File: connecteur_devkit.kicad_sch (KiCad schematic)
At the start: 8 parts, among them J10 OLED_SPI_2x8, J5 DEVKIT_C2000_ROW_A, J6 DEVKIT_C2000_ROW_B, J7 ESP32_C6_DEVKITC_1_J1, J8 ESP32_C6_DEVKITC_1_J3, U4 ER-OLEDM032-1

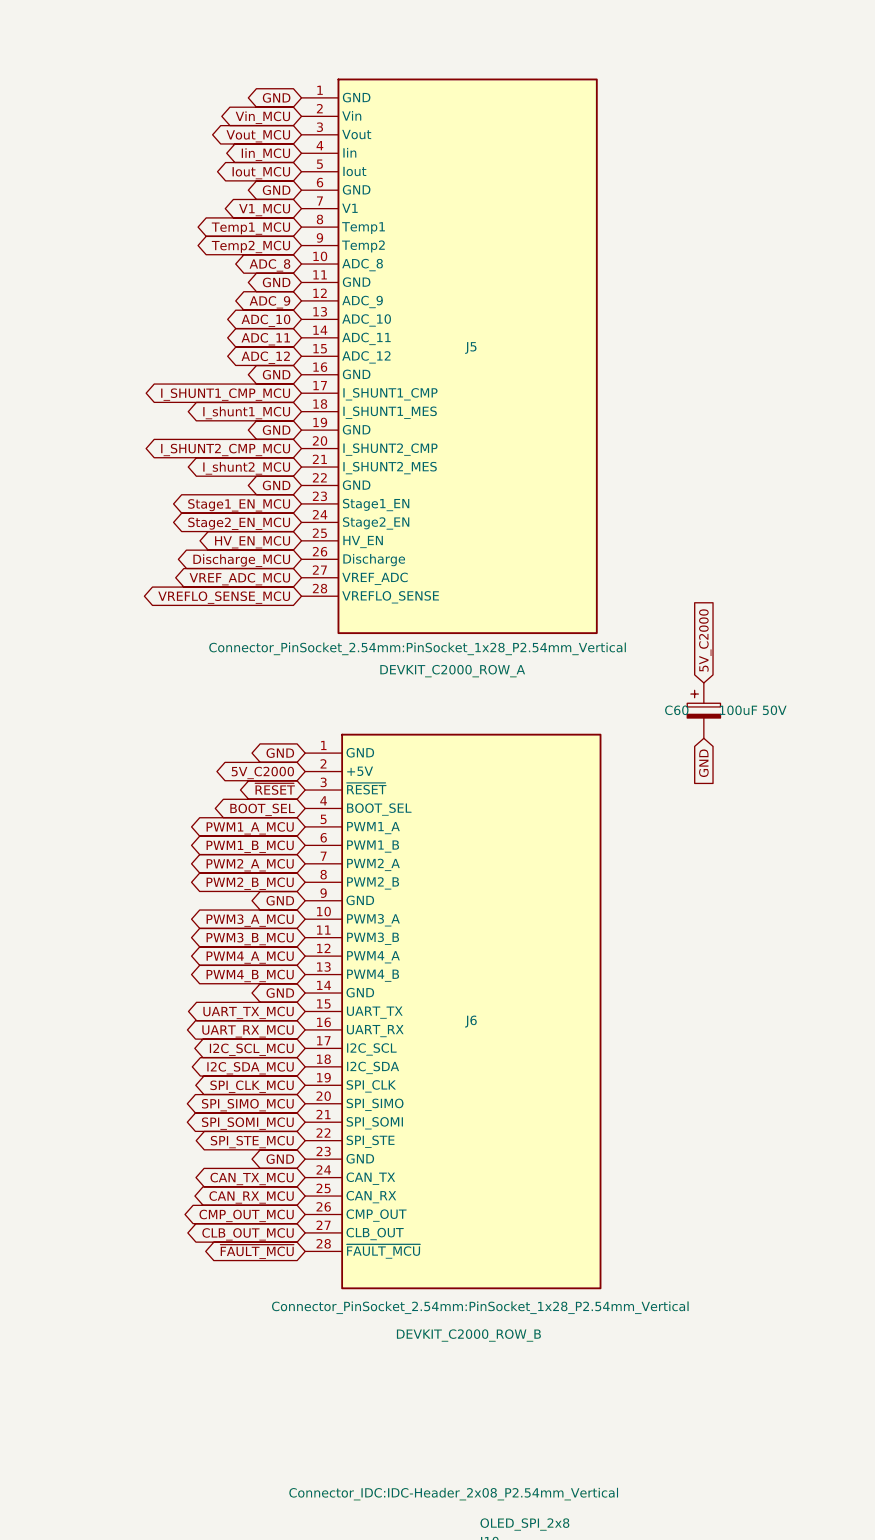
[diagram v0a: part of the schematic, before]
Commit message: Remplace le connecteur devkit par le nouveau connecteur devkit_B (2x24/2x24)
devkit_B_F28P551 est passe a deux embases 2x24 (une par domaine, masse
en vis-a-vis de chaque signal pour reduire l'inductance de boucle),
construit cote KICAD-C2000-devkit a partir du plan v2
(doc/connecteur-v2-plan.md la-bas). Remplace DEVKIT_C2000_ROW_A/ROW_B
(1x28 chacun) par DEVKIT_C2000_A/DEVKIT_C2000_B sur ce shield (J17/J18,
footprint PinSocket_2x24_P2.54mm_Vertical).

Remplacement pur : les 96 nouveaux noms de broche retombent tous dans
la table deja construite depuis les 56 anciennes etiquettes reelles
(verifie, pas suppose) - aucun renommage de net, aucune modification
attendue dans les nappes/protections. devkit_A_F280037 n'est plus
compatible avec ce shield tant qu'il n'a pas recu la meme mise a jour
(decision #25, meme logique que la decision #13 cote devkit).

Deux bugs trouves et corriges pendant la generation (noms de net bruts
au lieu des vrais noms projet avec suffixe _MCU ; broches no_connect
etiquetees au lieu d'un marqueur dedie) - voir decision #25 pour le
detail. Verifie avec check_schematic_labels.py et kicad-cli sch erc
feuille par feuille : aucune categorie nouvelle, aucune augmentation
ailleurs que sur les reserves deja connues.

Co-Authored-By: Claude Sonnet 5 <noreply@anthropic.com>
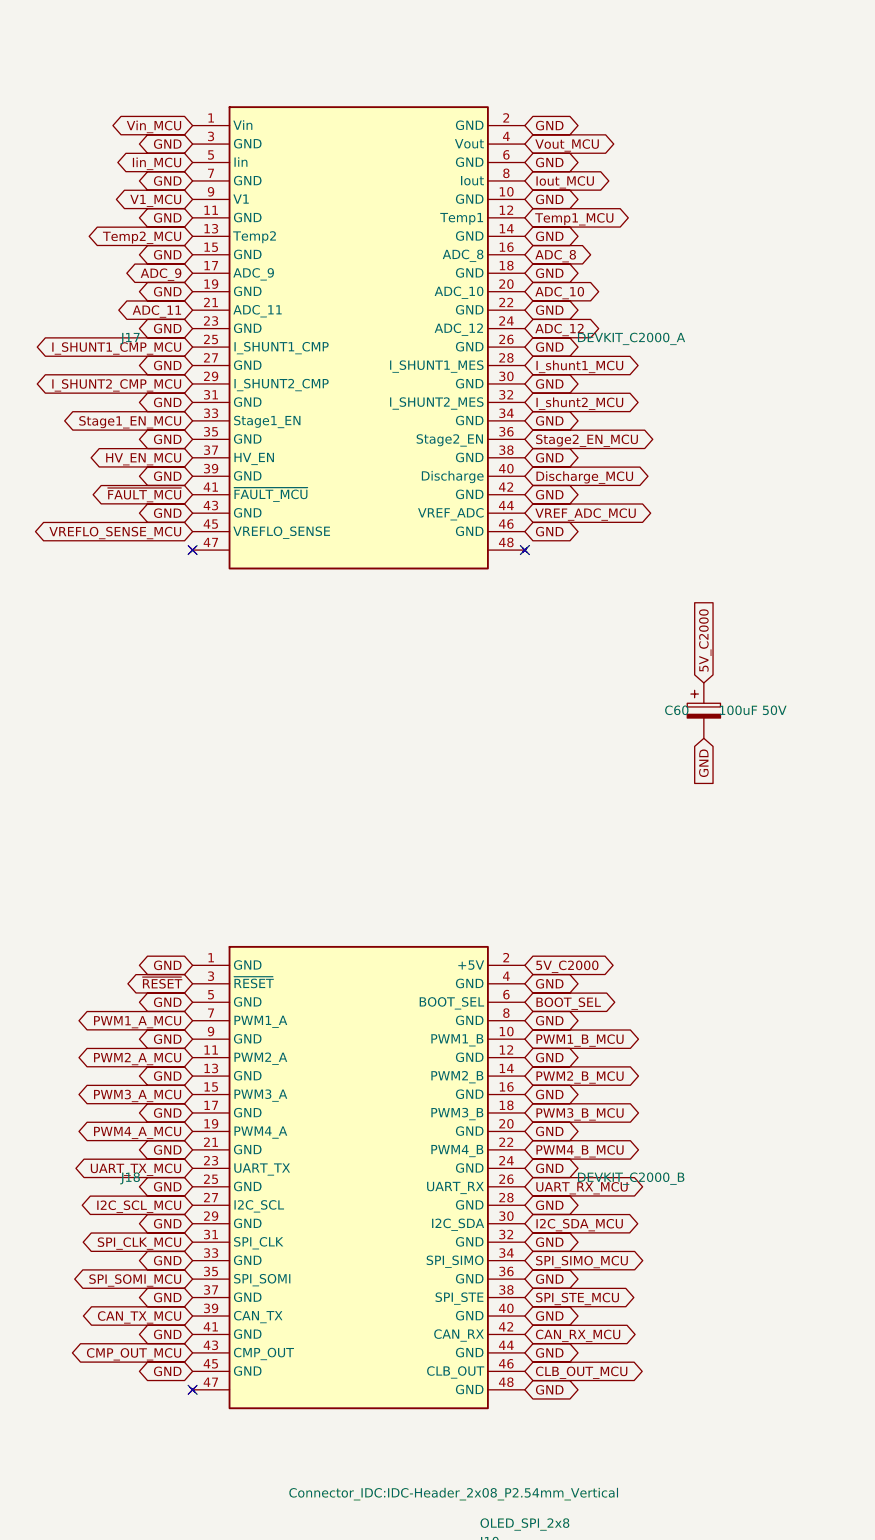
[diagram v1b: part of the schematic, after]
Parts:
- removed J5: DEVKIT_C2000_ROW_A, Connector_PinSocket_2.54mm:PinSocket_1x28_P2.54mm_Vertical, symbol C2000_Devkit_Connectors:DEVKIT_C2000_ROW_A
- removed J6: DEVKIT_C2000_ROW_B, Connector_PinSocket_2.54mm:PinSocket_1x28_P2.54mm_Vertical, symbol C2000_Devkit_Connectors:DEVKIT_C2000_ROW_B
- added J17: DEVKIT_C2000_A, Connector_PinSocket_2.54mm:PinSocket_2x24_P2.54mm_Vertical, symbol C2000_Devkit_Connectors:DEVKIT_C2000_A
- added J18: DEVKIT_C2000_B, Connector_PinSocket_2.54mm:PinSocket_2x24_P2.54mm_Vertical, symbol C2000_Devkit_Connectors:DEVKIT_C2000_B
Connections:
- net 5V_C2000: now also J18.2 (+5V)
- net ADC_10: now also J17.20 (ADC_10)
- net ADC_11: now also J17.21 (ADC_11)
- net ADC_12: now also J17.24 (ADC_12)
- net ADC_8: now also J17.16 (ADC_8)
- net ADC_9: now also J17.17 (ADC_9)
- net BOOT_SEL: now also J18.6 (BOOT_SEL)
- net CAN_RX_MCU: now also J18.42 (CAN_RX)
- net CAN_TX_MCU: now also J18.39 (CAN_TX)
- net CLB_OUT_MCU: now also J18.46 (CLB_OUT)
- net CMP_OUT_MCU: now also J18.43 (CMP_OUT)
- net Discharge_MCU: now also J17.40 (Discharge)
- net GND: now also J17.10 (GND), J17.11 (GND), J17.14 (GND), J17.15 (GND), J17.18 (GND), J17.19 (GND), J17.2 (GND), J17.22 (GND), J17.23 (GND), J17.26 (GND), J17.27 (GND), J17.3 (GND), J17.30 (GND), J17.31 (GND), J17.34 (GND), J17.35 (GND), J17.38 (GND), J17.39 (GND), J17.42 (GND), J17.43 (GND), J17.46 (GND), J17.6 (GND), J17.7 (GND), J18.1 (GND), J18.12 (GND), J18.13 (GND), J18.16 (GND), J18.17 (GND), J18.20 (GND), J18.21 (GND), J18.24 (GND), J18.25 (GND), J18.28 (GND), J18.29 (GND), J18.32 (GND), J18.33 (GND), J18.36 (GND), J18.37 (GND), J18.4 (GND), J18.40 (GND), J18.41 (GND), J18.44 (GND), J18.45 (GND), J18.48 (GND), J18.5 (GND), J18.8 (GND), J18.9 (GND)
- net HV_EN_MCU: now also J17.37 (HV_EN)
- net I2C_SCL_MCU: now also J18.27 (I2C_SCL)
- net I2C_SDA_MCU: now also J18.30 (I2C_SDA)
- net I_SHUNT1_CMP_MCU: now also J17.25 (I_SHUNT1_CMP)
- net I_SHUNT2_CMP_MCU: now also J17.29 (I_SHUNT2_CMP)
- net I_shunt1_MCU: now also J17.28 (I_SHUNT1_MES)
- net I_shunt2_MCU: now also J17.32 (I_SHUNT2_MES)
- net Iin_MCU: now also J17.5 (Iin)
- net Iout_MCU: now also J17.8 (Iout)
- net PWM1_A_MCU: now also J18.7 (PWM1_A)
- net PWM1_B_MCU: now also J18.10 (PWM1_B)
- net PWM2_A_MCU: now also J18.11 (PWM2_A)
- net PWM2_B_MCU: now also J18.14 (PWM2_B)
- net PWM3_A_MCU: now also J18.15 (PWM3_A)
- net PWM3_B_MCU: now also J18.18 (PWM3_B)
- net PWM4_A_MCU: now also J18.19 (PWM4_A)
- net PWM4_B_MCU: now also J18.22 (PWM4_B)
- net SPI_CLK_MCU: now also J18.31 (SPI_CLK)
- net SPI_SIMO_MCU: now also J18.34 (SPI_SIMO)
- net SPI_SOMI_MCU: now also J18.35 (SPI_SOMI)
- net SPI_STE_MCU: now also J18.38 (SPI_STE)
- net Stage1_EN_MCU: now also J17.33 (Stage1_EN)
- net Stage2_EN_MCU: now also J17.36 (Stage2_EN)
- net Temp1_MCU: now also J17.12 (Temp1)
- net Temp2_MCU: now also J17.13 (Temp2)
- net UART_RX_MCU: now also J18.26 (UART_RX)
- net UART_TX_MCU: now also J18.23 (UART_TX)
- net V1_MCU: now also J17.9 (V1)
- net VREFLO_SENSE_MCU: now also J17.45 (VREFLO_SENSE)
- net VREF_ADC_MCU: now also J17.44 (VREF_ADC)
- net Vin_MCU: now also J17.1 (Vin)
- net Vout_MCU: now also J17.4 (Vout)
- net ~{FAULT_MCU}: now also J17.41 (~{FAULT_MCU})
- net ~{RESET}: now also J18.3 (~{RESET})
- no-connect marks 0 -> 3
